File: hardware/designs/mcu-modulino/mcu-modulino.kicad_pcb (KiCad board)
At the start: 4 copper layers, 68.9 x 53.3 mm, 164 parts, among them J1 USB_C_Receptacle_USB2.0_14P, J2 FTDI Header, J4 PROG, J5 JTAG, J6 Stemma QT, Q1 BC847BDW1, SW1 RESET, SW2 BOOT, U1 CP2102N-Axx-xQFN28, U2 NCP1117-3.3_SOT223, U3 ESP32-WROVER-E, U4 IS31FL3731-QF, X1 EYESPI, X2 EYESPI, X3 EYESPI

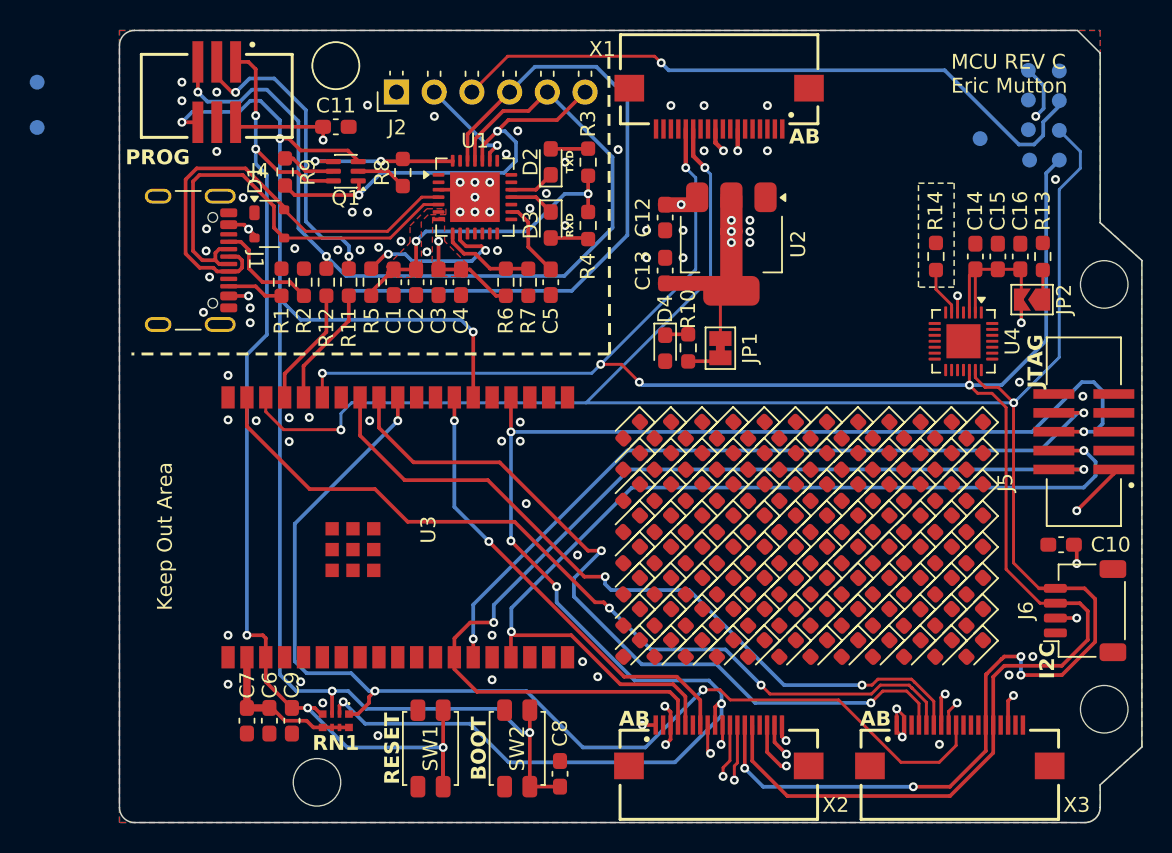
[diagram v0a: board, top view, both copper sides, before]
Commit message: feat: remove charlieplex matrix from board rev c
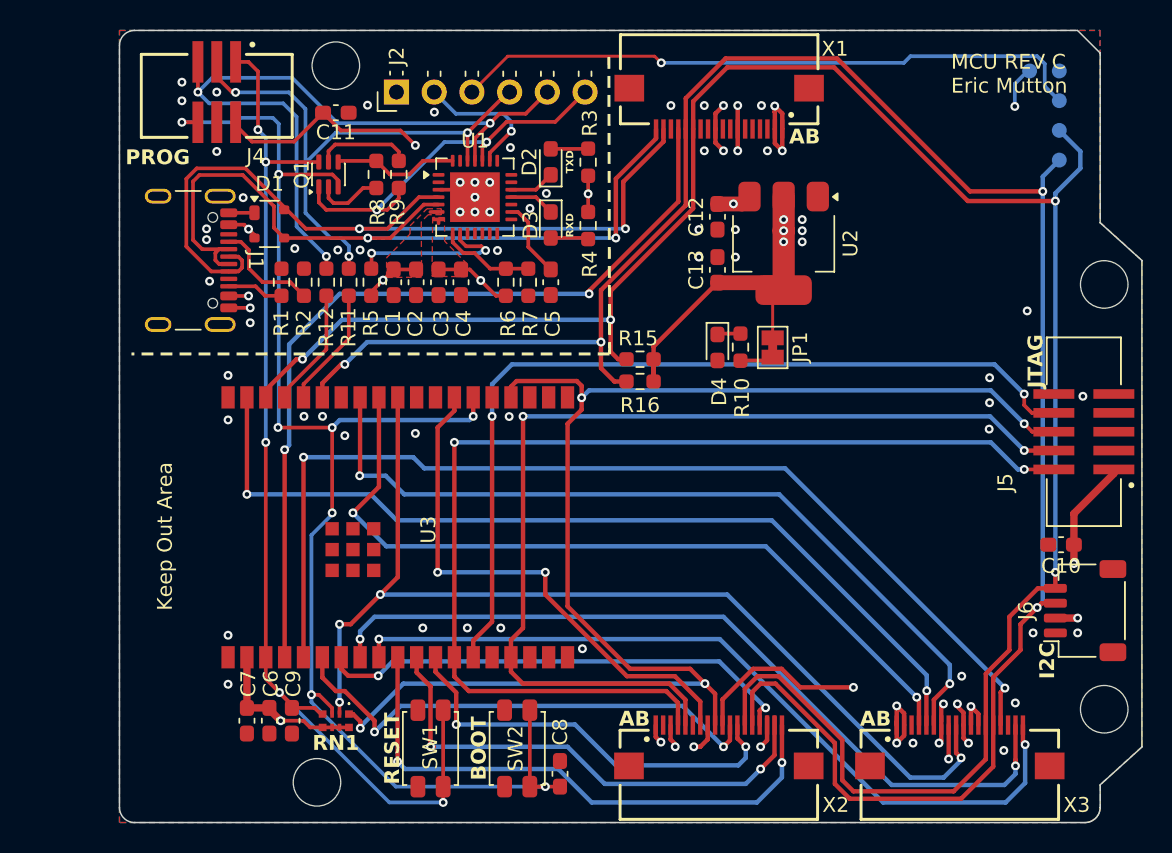
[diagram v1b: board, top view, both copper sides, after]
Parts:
- removed C14: 0.1uF, Capacitor_SMD:C_0603_1608Metric_Pad1.08x0.95mm_HandSolder
- removed C15, C16: 10uF, Capacitor_SMD:C_0603_1608Metric_Pad1.08x0.95mm_HandSolder
- removed D301, D302, D303, D304, D305, D306, D307, D308, D309, D310, D311, D312, D313, D314, D315, D316, D317, D318, D319, D320, D321, D322, D323, D324, D325, D326, D327, D328, D329, D330, D331, D332, D333, D334, D335, D336, D337, D338, D339, D340, D341, D342, D343, D344, D345, D346, D347, D348, D349, D350, D351, D352, D353, D354, D355, D356, D357, D358, D359, D360, D361, D362, D363, D364, D365, D366, D367, D368, D369, D370, D371, D372, D373, D374, D375, D376, D377, D378, D379, D380, D381, D382, D383, D384, D385, D386, D387, D388, D389, D390, D391, D392, D393, D394, D395, D396: XHY-STB0603SR, LED_SMD:LED_0603_1608Metric
- removed JP2: AD, Jumper:SolderJumper-2_P1.3mm_Open_TrianglePad1.0x1.5mm
- removed R13, R14: 10k, Resistor_SMD:R_0603_1608Metric_Pad0.98x0.95mm_HandSolder
- removed TP1, TP2, TP3, TP4, TP5, TP6: TestPoint, TestPoint:TestPoint_Pad_D1.0mm
- removed U4: IS31FL3731-QF, Package_DFN_QFN:QFN-28-1EP_4x4mm_P0.4mm_EP2.3x2.3mm
- added R15: 4.7k, Resistor_SMD:R_0603_1608Metric_Pad0.98x0.95mm_HandSolder, F.Cu at (150.1, 99.7)
- added R16: 4.7k, Resistor_SMD:R_0603_1608Metric_Pad0.98x0.95mm_HandSolder, F.Cu at (150.1, 101.2)
- moved R9 7.66 mm to (133.9, 87.2)
- moved JP1 3.52 mm to (159.1, 98.9)
- moved R10 3.52 mm to (156.9, 98.8)
- moved U2 3.52 mm to (159.8, 91.8)
- moved C12 3.52 mm to (155.3, 90.1)
- moved C13 3.52 mm to (155.3, 93.6)
- moved D4 3.52 mm to (155.3, 98.9)
- moved R8 1.79 mm to (132.4, 87.2)
- moved Q1 1.18 mm to (129.2, 87.2), turned to 90 degrees
- moved C11 0.95 mm to (129.6, 83.1)
- moved REF** 0.20 mm to (119.8, 92.3)
- moved TP10 0.09 mm to (176.4, 80.2)
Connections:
- RN1 pad 1: Net-(U3B-IO5) -> /HSPI_CS
- RN1 pad 2: Net-(U3B-MTDO) -> /VSPI_CS
- X3 pad 10: GND -> +3.3V
- X3 pad 16: +3.3V -> GND
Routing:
- net /RF_INT: track 0.00 -> 69.8 mm, vias 0 -> 2
- net /BMS_INT: track 0.00 -> 56.4 mm, vias 0 -> 2
- net /VSPI_GDO0: track 0.00 -> 54.6 mm, vias 0 -> 2
- net /VSPI_GDO2: track 0.00 -> 53.8 mm, vias 0 -> 2
- net /LRCLK: track 1.68 -> 38.3 mm, vias 1 -> 2
- net /HMI_INT: track 0.00 -> 32.7 mm, vias 0 -> 2
- net /BCLK: track 2.80 -> 34.2 mm, vias 1 -> 2
- net /DIN: track 3.65 -> 33.8 mm, vias 1 -> 2
- net /TXD: track 66.3 -> 36.7 mm, vias 2 -> 3
- net /D-: track 29.2 -> 54.5 mm, vias 0 -> 2
- net /D+: track 31.1 -> 56.2 mm, vias 0 -> 2
- net /DOUT: track 3.80 -> 28.4 mm, vias 1 -> 2
- net +3.3V: track 102.4 -> 125.4 mm, vias 18 -> 23
- net VBUS: track 99.3 -> 113.8 mm
- net /HSPI_CS: track 108.0 -> 94.6 mm, vias 6 -> 4
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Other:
- board text added: "2-WAY RADIO IFACE B2B"
- board text added: "BATTERY POWER IFACE B2B"
- board text added: "HSPI+I2C0+I2S0"
- board text added: "HUMAN-MACHINE IFACE B2B"
- board text added: "I2C0"
- board text added: "VSPI+I2C0"
- board text removed: "FTDI UART HEADER"
- board text removed: "HMI CONN"
- board text removed: "POWER CONN"
- board text removed: "RF CONN"
- board text removed: "RX"
- board text removed: "TX"
- board text removed: "VBUS"
- board text removed: "~{CTS}"
- board text removed: "~{RTS}"
